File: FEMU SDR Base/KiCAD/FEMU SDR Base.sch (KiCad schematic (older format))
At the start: 46 parts, among them P1 Battery, P10 PWM_In_2, P11 PWM_In_3, P12 PWM_In_4, P13 PWM_Out_1, P14 PWM_Out_2, P15 PWM_Out_2, P16 PWM_Out_2, P17 SDR_1_USB, P18 SDR_2_USB, P2 SDR_Shield_1, P3 SDR_Shield_2, P4 ESC_1, P5 ESC_2, P6 ESC_3, P7 ESC_4, P8 Raspi_Power_Shield, P9 PWM_In_1, U1 TPS562209, U2 SDR_1_LDO_1_2V, U3 SDR_2_LDO_1_2V, U4 SDR_1_LDO_3_3V, U5 SDR_2_LDO_3_3V

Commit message: STATUS = FREE, RASPI PSU smaller layout, footprints swapped
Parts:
- P8: footprint ARB_foots:PCB_Shield_29x25mm -> ARB_foots:PCB_Shield_35x20mm
- R1, R2: footprint Resistors_SMD:R_0805_HandSoldering -> Resistors_SMD:R_0603_HandSoldering
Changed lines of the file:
@@
 F 0 "R1" V 2630 1350 50  0000 C CNN
 F 1 "100" V 2550 1350 50  0000 C CNN
-F 2 "Resistors_SMD:R_0805_HandSoldering" V 2480 1350 50  0001 C CNN
+F 2 "Resistors_SMD:R_0603_HandSoldering" V 2480 1350 50  0001 C CNN
 F 3 "" H 2550 1350 50  0000 C CNN
 	1    2550 1350
@@
 F 0 "R2" V 3830 1350 50  0000 C CNN
 F 1 "10k" V 3750 1350 50  0000 C CNN
-F 2 "Resistors_SMD:R_0805_HandSoldering" V 3680 1350 50  0001 C CNN
+F 2 "Resistors_SMD:R_0603_HandSoldering" V 3680 1350 50  0001 C CNN
 F 3 "" H 3750 1350 50  0000 C CNN
 	1    3750 1350
@@
 F 0 "P8" H 2400 5000 50  0000 C CNN
 F 1 "Raspi_Power_Shield" V 2500 4900 50  0000 C CNN
-F 2 "ARB_foots:PCB_Shield_29x25mm" H 2400 4900 50  0001 C CNN
+F 2 "ARB_foots:PCB_Shield_35x20mm" H 2400 4900 50  0001 C CNN
 F 3 "" H 2400 4900 50  0000 C CNN
 	1    2400 4900

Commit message: Added pads for power, usb and pwm distribution
Signed-off-by: hardiepienaar <hardiepienaar@gmail.com>
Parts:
- removed P17: SDR_1_USB, symbol CONN_01X03
- removed P18: SDR_2_USB, symbol CONN_01X03
- removed P4: ESC_1, symbol CONN_01X02
- removed P5: ESC_2, symbol CONN_01X02
- removed P6: ESC_3, symbol CONN_01X02
- removed P7: ESC_4, symbol CONN_01X02
- added P17, P19, P4, P6: 12V, SMD_Packages:1Pin, symbol CONN_01X01
- added P18, P20, P5, P7: GND, SMD_Packages:1Pin, symbol CONN_01X01
- added P21: S0GND, SMD_Packages:1Pin, symbol CONN_01X01
- added P22: S1GND, SMD_Packages:1Pin, symbol CONN_01X01
- added P23: S0DN, SMD_Packages:1Pin, symbol CONN_01X01
- added P24: S1DN, SMD_Packages:1Pin, symbol CONN_01X01
- added P25: S0DP, SMD_Packages:1Pin, symbol CONN_01X01
- added P26: S1DP, SMD_Packages:1Pin, symbol CONN_01X01
- added P27, P31: PWM0, SMD_Packages:SMD-1206_Pol, symbol CONN_01X02
- added P28, P32: PWM5, SMD_Packages:SMD-1206_Pol, symbol CONN_01X02
- added P29, P33: PWM6, SMD_Packages:SMD-1206_Pol, symbol CONN_01X02
- added P30, P34: PWM7, SMD_Packages:SMD-1206_Pol, symbol CONN_01X02
- P10: value PWM_In_2 -> PWM2; footprint (none) -> SMD_Packages:SMD-1206_Pol
- P11: value PWM_In_3 -> PWM3; footprint (none) -> SMD_Packages:SMD-1206_Pol
- P12: value PWM_In_4 -> PWM4; footprint (none) -> SMD_Packages:SMD-1206_Pol
- P13: value PWM_Out_1 -> PWM1; footprint (none) -> SMD_Packages:SMD-1206_Pol
- P14: value PWM_Out_2 -> PWM2; footprint (none) -> SMD_Packages:SMD-1206_Pol
- P15: value PWM_Out_2 -> PWM3; footprint (none) -> SMD_Packages:SMD-1206_Pol
- P16: value PWM_Out_2 -> PWM4; footprint (none) -> SMD_Packages:SMD-1206_Pol
- P9: value PWM_In_1 -> PWM1; footprint (none) -> SMD_Packages:SMD-1206_Pol
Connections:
- net labels removed: Earth
- wire segments 87 -> 97
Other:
- note added: "Add ESC wire holds\n"
- moved on the sheet: P10, P11, P12, P13, P14, P15, P16, P2, P3, P8, P9

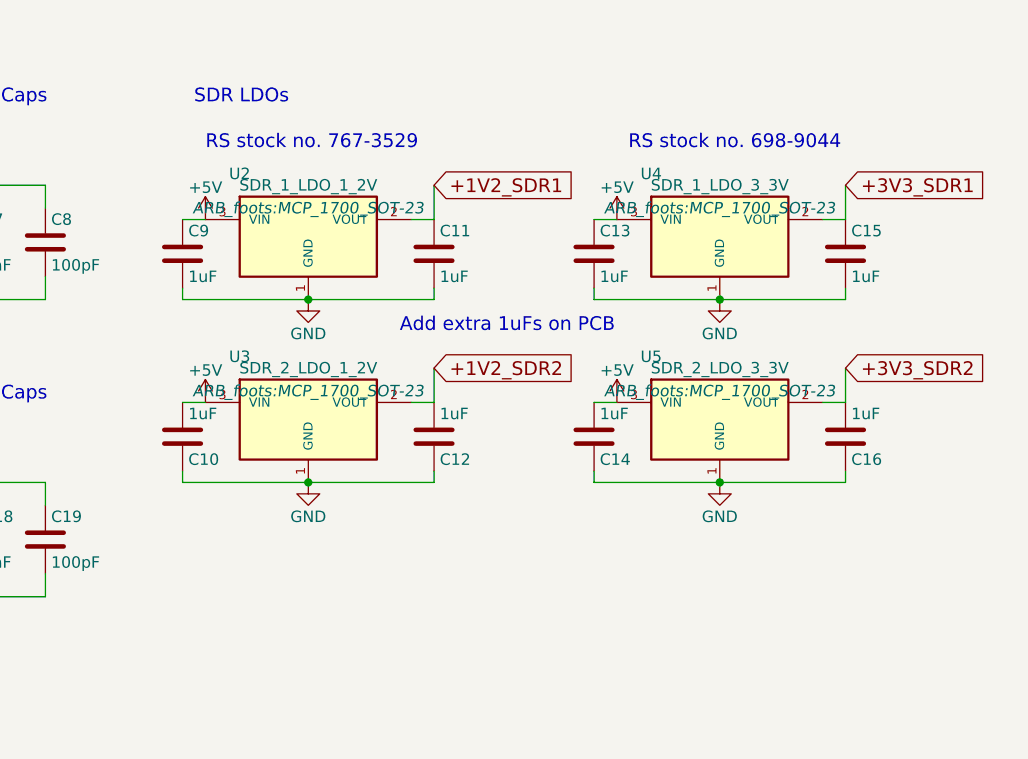
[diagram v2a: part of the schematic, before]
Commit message: STATUS=FREE, RasPi Power fit in
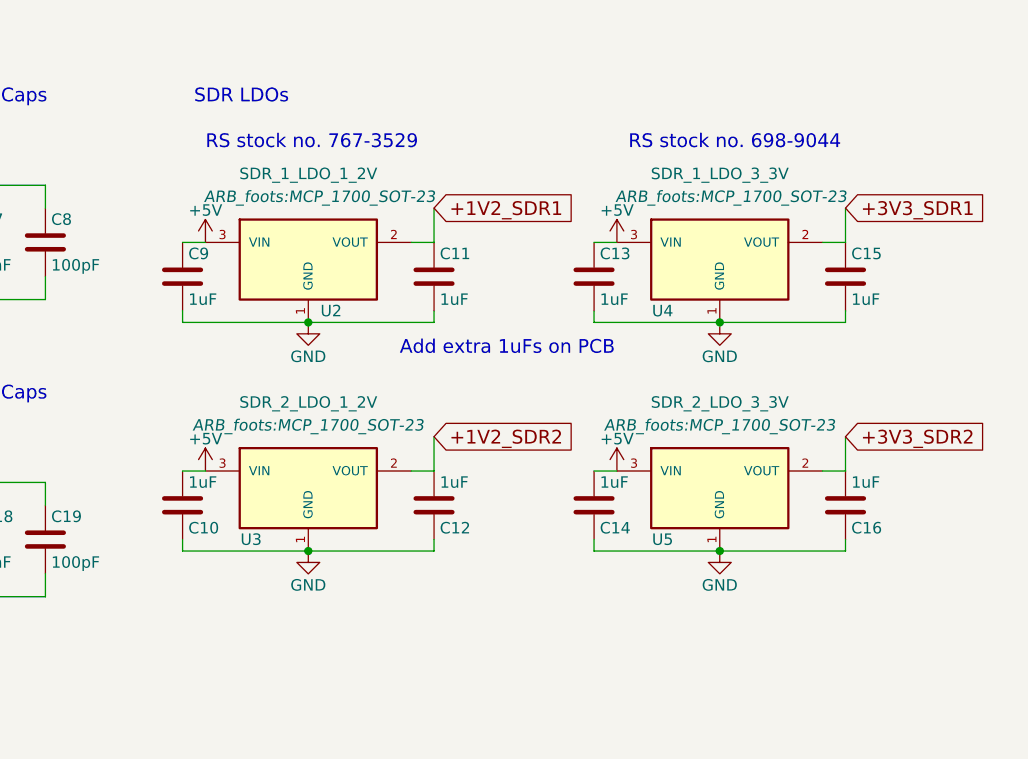
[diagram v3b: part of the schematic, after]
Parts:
- P8: footprint ARB_foots:PCB_Shield_35x20mm -> ARB_foots:PCB_Shield_26x16mm
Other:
- moved on the sheet: C10, C11, C12, C13, C14, C15, C16, C9, U2, U3, U4, U5

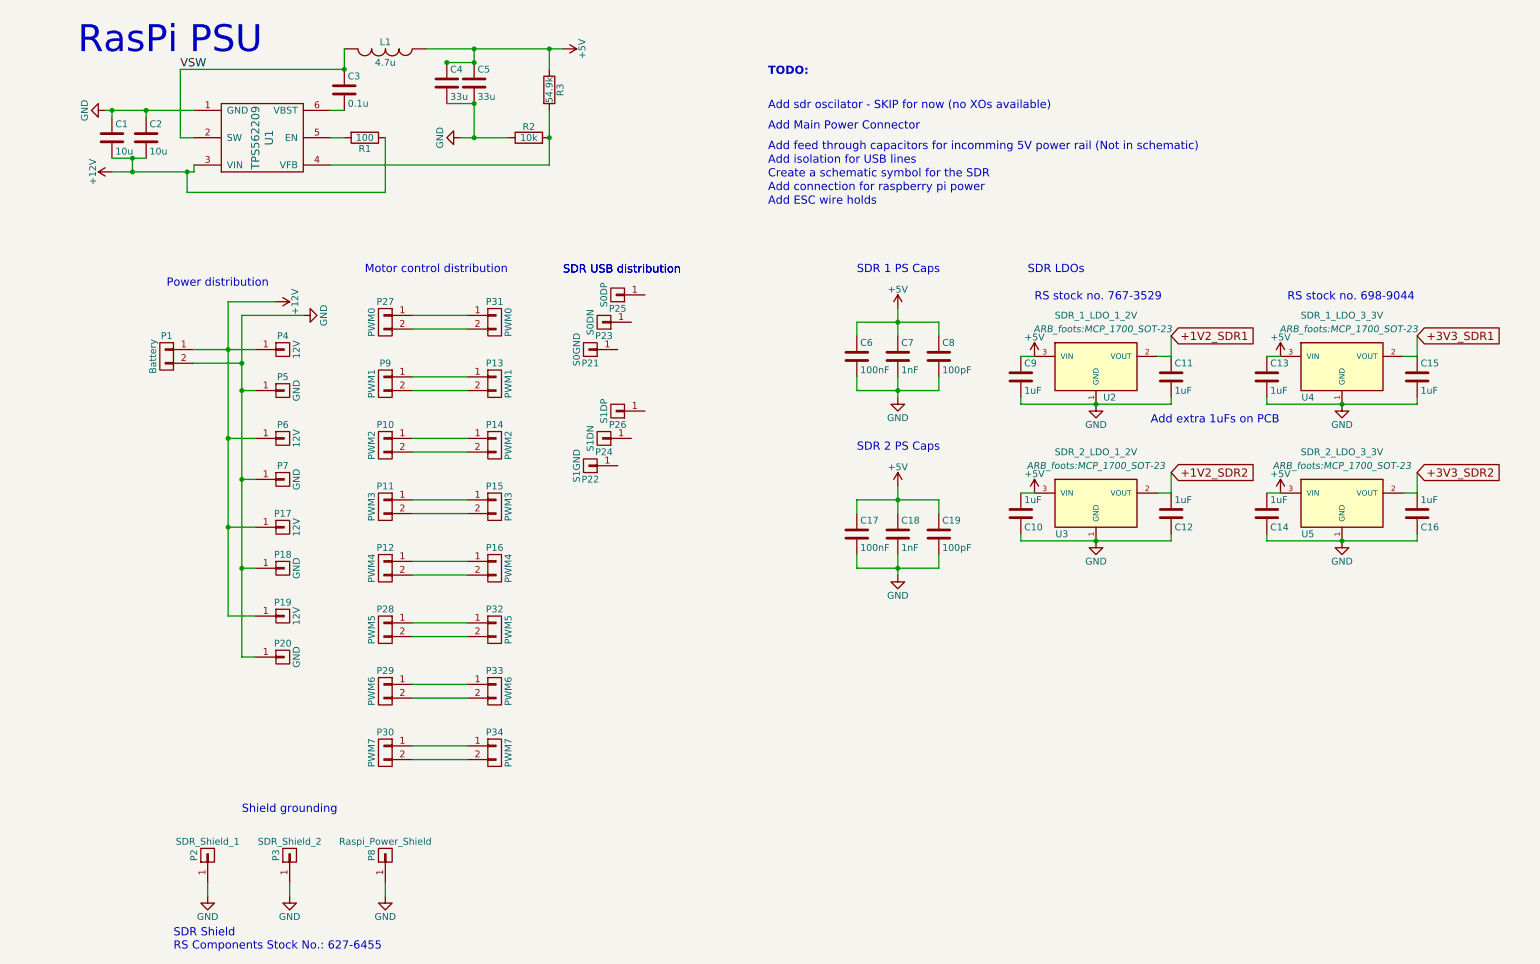
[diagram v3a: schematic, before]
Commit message: STATUS=FREE, Redo of RaspiPSU to avoid zone errors, trace start for +5V
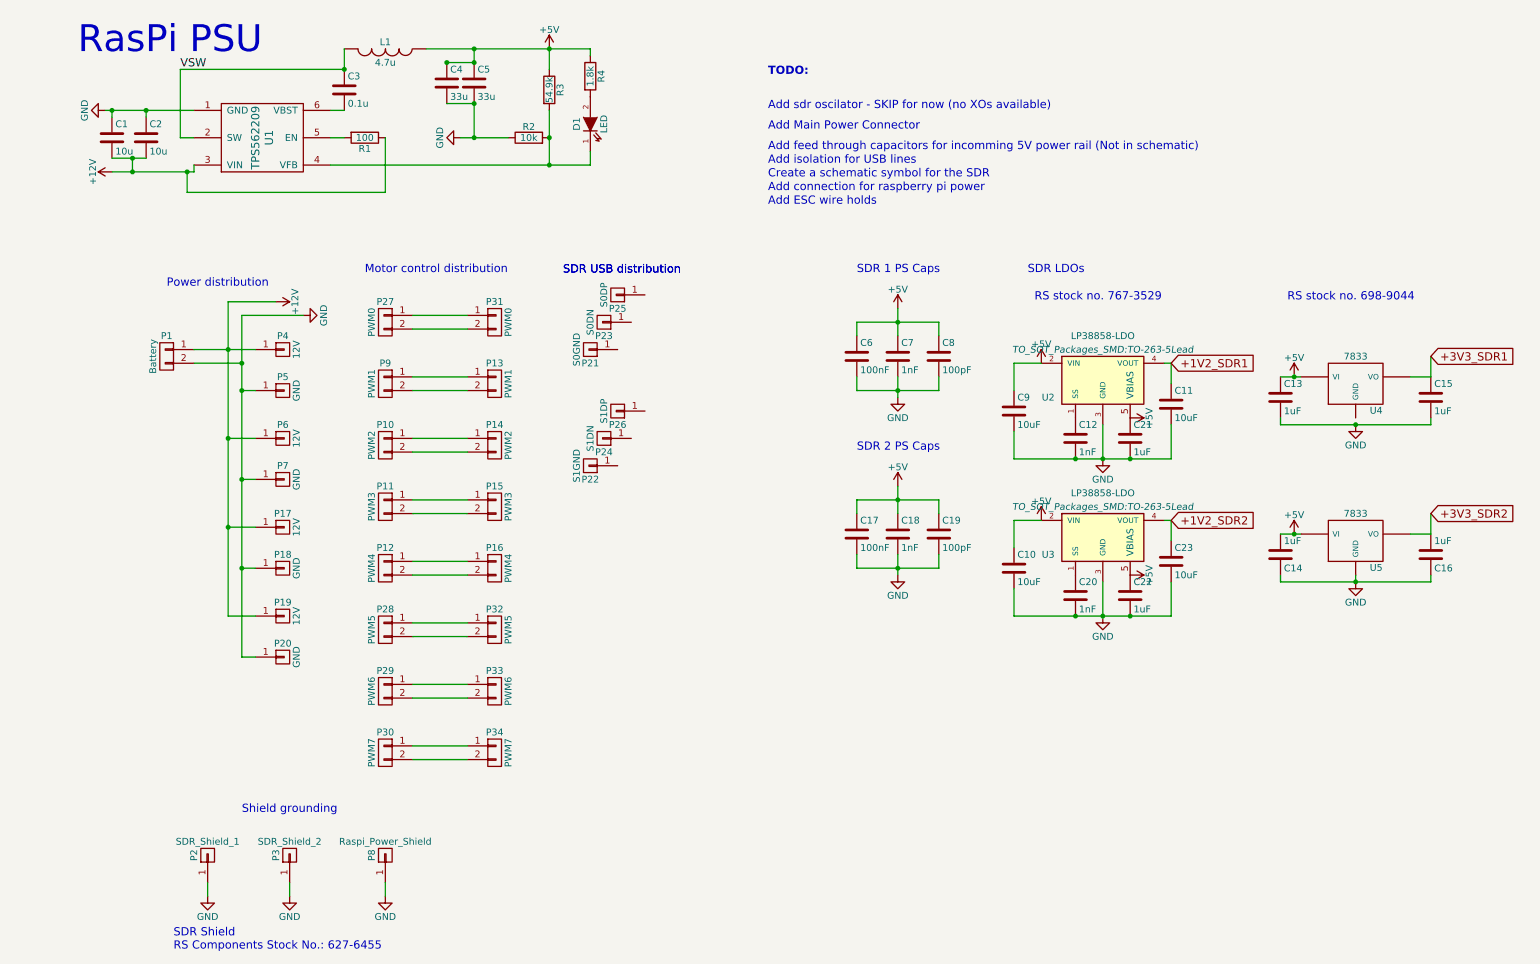
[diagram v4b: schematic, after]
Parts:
- removed U2: SDR_1_LDO_1_2V, ARB_foots:MCP_1700_SOT-23, symbol APE8865N-12-HF-3
- removed U3: SDR_2_LDO_1_2V, ARB_foots:MCP_1700_SOT-23, symbol APE8865N-12-HF-3
- removed U4: SDR_1_LDO_3_3V, ARB_foots:MCP_1700_SOT-23, symbol APE8865N-33-HF-3
- removed U5: SDR_2_LDO_3_3V, ARB_foots:MCP_1700_SOT-23, symbol APE8865N-33-HF-3
- added C20: 1nF, Capacitors_SMD:C_0805_HandSoldering, symbol C
- added C21, C22: 1uF, Capacitors_SMD:C_0805_HandSoldering, symbol C
- added C23: 10uF, Capacitors_SMD:C_0805_HandSoldering, symbol C
- added D1: LED, LEDs:LED_0805, symbol LED
- added R4: 1.8k, Capacitors_SMD:C_0805_HandSoldering, symbol R
- added U2, U3: LP38858-LDO, TO_SOT_Packages_SMD:TO-263-5Lead, symbol LP38858-LDO
- added U4, U5: 7833, TO_SOT_Packages_SMD:TO-252-2Lead, symbol 7833
- C10, C11, C9: value 1uF -> 10uF
- C12: value 1uF -> 1nF
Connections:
- net +1V2_SDR1: now also U2.4 (VOUT)
- net +1V2_SDR2: now also C23.1, U3.4 (VOUT); no longer C12.2
- net +3V3_SDR1: now also U4.VO
- net +3V3_SDR2: now also U5.VO
- net +5V: now also C10.1, C21.1, C22.1, R4.1, U2.2 (VIN), U2.5 (VBIAS), U3.2 (VIN), U3.5 (VBIAS), U4.VI, U5.VI; no longer C10.2
- net GND: now also C10.2, C12.2, C20.2, C21.2, C22.2, C23.2, U2.3 (GND), U3.3 (GND), U5.GND; no longer C10.1, C12.1
- net at R2.2, R3.2, U1.4 (VFB): now also D1.1 (K)
- new net: C12.1, U2.1 (SS)
- new net: D1.2 (A), R4.2
- new net: C20.1, U3.1 (SS)
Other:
- note removed: "Add extra 1uFs on PCB"
- moved on the sheet: C11, C13, C14, C15, C16, C9

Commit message: Added power connections, power routing, GND isolation and cable tray grounding
Signed-off-by: hardiepienaar <hardiepienaar@gmail.com>
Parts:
- added P35: Battery, Misc footprints:XT60, symbol CONN_01X02
- P1: footprint (none) -> Misc footprints:XT60
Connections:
- net +12V: now also P1.2 (P2), P35.2 (P2); no longer P1.1 (P1)
- net GND: now also P1.1 (P1), P35.1 (P1); no longer P1.2 (P2)
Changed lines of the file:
@@
 F 0 "P1" H 1100 3100 50  0000 C CNN
 F 1 "Battery" V 1200 2950 50  0000 C CNN
-F 2 "" H 1100 2950 50  0001 C CNN
+F 2 "Misc footprints:XT60" H 1100 2950 50  0001 C CNN
 F 3 "" H 1100 2950 50  0000 C CNN
 	1    1100 2950
-	-1   0    0    -1
+	-1   0    0    1
 $EndComp
 $Comp
@@
 Connection ~ 1550 2900
 Wire Wire Line
-	1300 3000 1650 3000
-Wire Wire Line
 	1650 2650 1650 5150
 Wire Wire Line
@@
 Wire Wire Line
 	4200 1550 4200 1450
+$Comp
+L CONN_01X02 P35
+U 1 1 5736ACD2
+P 1100 3450
+F 0 "P35" H 1100 3600 50  0000 C CNN
+F 1 "Battery" V 1200 3450 50  0000 C CNN
+F 2 "Misc footprints:XT60" H 1100 3450 50  0001 C CNN
+F 3 "" H 1100 3450 50  0000 C CNN
+	1    1100 3450
+	-1   0    0    1
+$EndComp
+Wire Wire Line
+	1300 3400 1550 3400
+Connection ~ 1550 3400
+Wire Wire Line
+	1300 3500 1650 3500
+Connection ~ 1650 3500
+Wire Wire Line
+	1300 3000 1650 3000
 $EndSCHEMATC
